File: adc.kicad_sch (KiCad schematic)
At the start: 35 parts, among them U7 AD7177-2BRUZ, U70 TG2520SMN-16M-MCG, U75 OPA2189DGK

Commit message: Scan deleted.
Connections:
- net BufR+: no longer U7.22 (AIN1)
- net BufR-: no longer U7.23 (AIN2)
- no-connect marks 6 -> 8
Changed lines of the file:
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@@
 	)
 	(junction
-		(at 157.48 60.96)
-		(diameter 0)
-		(color 0 0 0 0)
-	)
-	(junction
-		(at 139.7 63.5)
-		(diameter 0)
-		(color 0 0 0 0)
-	)
-	(junction
 		(at 97.79 86.36)
 		(diameter 0)
@@
 	)
 	(no_connect
+		(at 168.91 48.26)
+	)
+	(no_connect
 		(at 199.39 63.5)
 	)
 	(no_connect
+		(at 168.91 50.8)
+	)
+	(no_connect
 		(at 199.39 45.72)
 	)
@@
 	(wire
 		(pts
-			(xy 139.7 48.26) (xy 139.7 63.5)
-		)
-		(stroke
-			(width 0)
-			(type default)
-		)
-	)
-	(wire
-		(pts
 			(xy 101.6 96.52) (xy 116.84 96.52)
 		)
@@
 	(wire
 		(pts
-			(xy 142.24 60.96) (xy 157.48 60.96)
+			(xy 142.24 60.96) (xy 168.91 60.96)
 		)
 		(stroke
@@
 	(wire
 		(pts
-			(xy 157.48 60.96) (xy 168.91 60.96)
-		)
-		(stroke
-			(width 0)
-			(type default)
-		)
-	)
-	(wire
-		(pts
 			(xy 91.44 86.36) (xy 97.79 86.36)
 		)
@@
 	(wire
 		(pts
-			(xy 157.48 50.8) (xy 157.48 60.96)
-		)
-		(stroke
-			(width 0)
-			(type default)
-		)
-	)
-	(wire
-		(pts
 			(xy 134.62 118.11) (xy 139.7 118.11)
 		)
@@
 	(wire
 		(pts
-			(xy 139.7 63.5) (xy 168.91 63.5)
-		)
-		(stroke
-			(width 0)
-			(type default)
-		)
-	)
-	(wire
-		(pts
 			(xy 200.66 48.26) (xy 214.63 48.26)
 		)
@@
 	(wire
 		(pts
-			(xy 139.7 48.26) (xy 168.91 48.26)
-		)
-		(stroke
-			(width 0)
-			(type default)
-		)
-	)
-	(wire
-		(pts
 			(xy 199.39 68.58) (xy 203.2 68.58)
 		)
@@
 	(wire
 		(pts
-			(xy 157.48 50.8) (xy 168.91 50.8)
-		)
-		(stroke
-			(width 0)
-			(type default)
-		)
-	)
-	(wire
-		(pts
 			(xy 175.26 105.41) (xy 186.69 105.41)
 		)
@@
 	(wire
 		(pts
-			(xy 135.89 63.5) (xy 139.7 63.5)
+			(xy 135.89 63.5) (xy 168.91 63.5)
 		)
 		(stroke
@@
 			)
 		)
-		(property "Datasheet" "50V"
+		(property "Datasheet" "X7R, 50V"
 			(at 139.7 106.68 0)
 			(effects
@@
 			)
 		)
-		(property "Datasheet" "50V"
+		(property "Datasheet" "X7R, 50V"
 			(at 139.7 114.3 0)
 			(effects

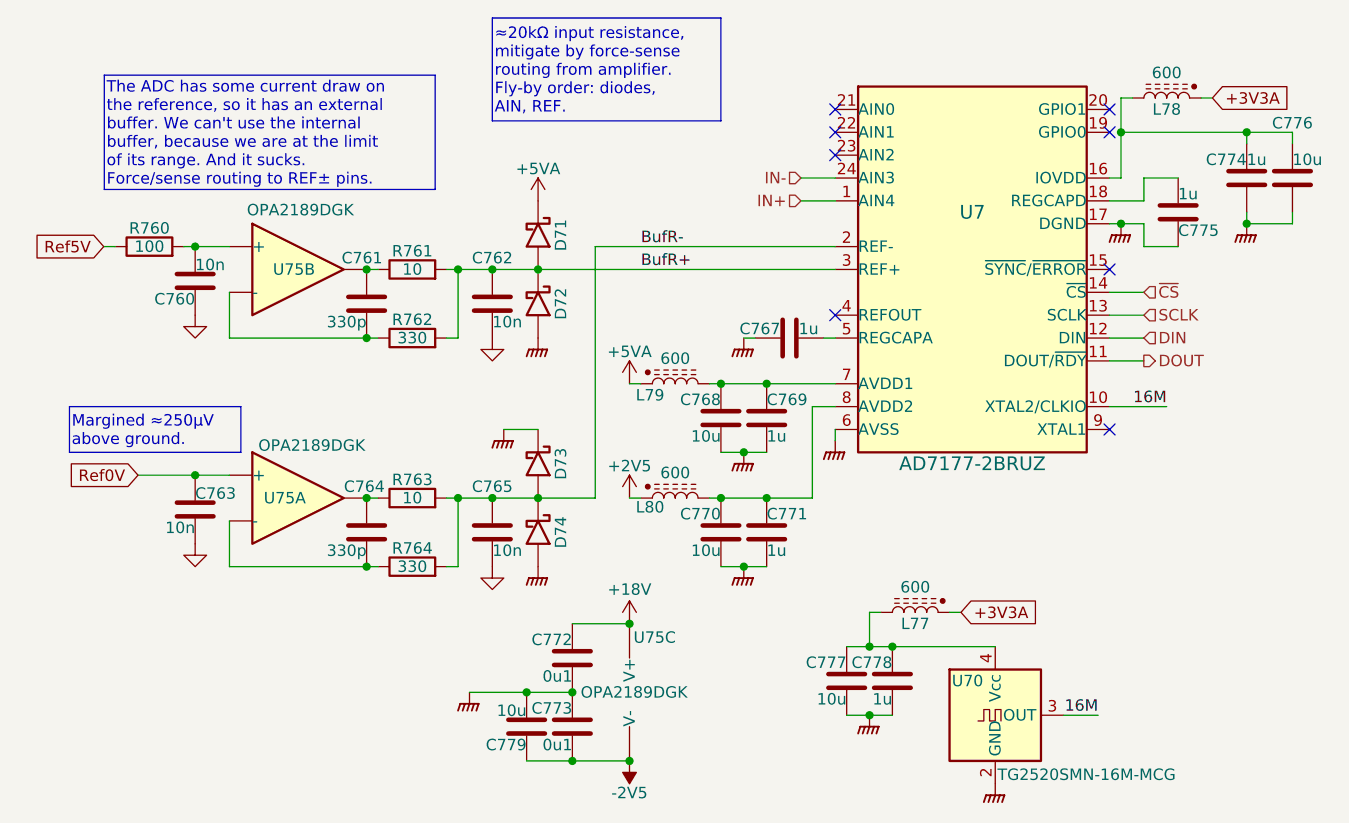
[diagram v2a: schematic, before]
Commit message: Put ref filtering into the schematic.
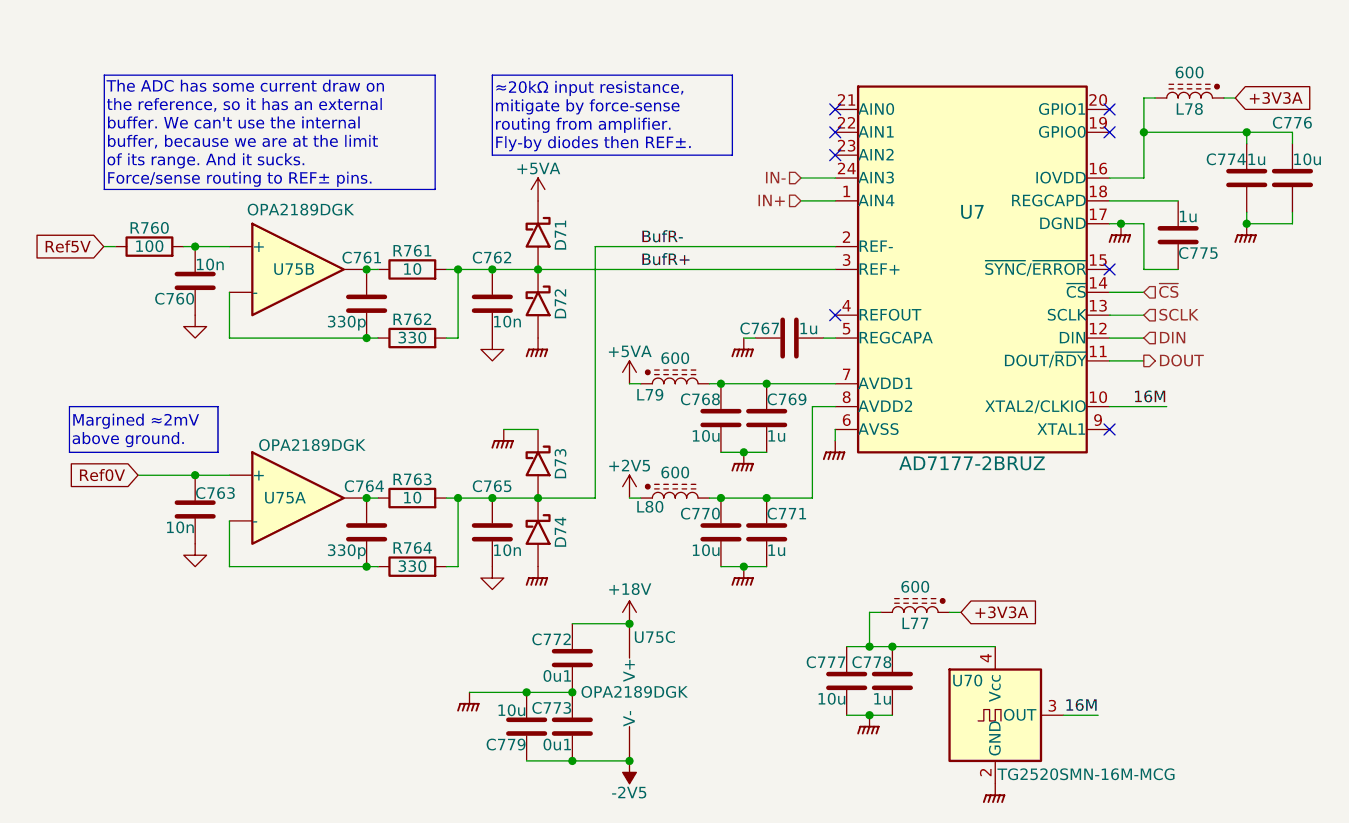
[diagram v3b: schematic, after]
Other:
- moved on the sheet: C775, L78
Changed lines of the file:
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@@
 	(generator_version "9.0")
 	(paper "A4")
-	(text_box "Margined ≈250µV above ground."
+	(text_box "Margined ≈2mV above ground."
 		(exclude_from_sim no)
 		(at 83.82 78.74 0)
-		(size 19.05 5.08)
+		(size 16.51 5.08)
 		(margins 0.254 0.254 0.254 0.254)
 		(stroke
@@
 		)
 	)
-	(text_box "≈20kΩ input resistance, mitigate by force-sense routing from amplifier.\nFly-by order: diodes, AIN, REF."
+	(text_box "≈20kΩ input resistance, mitigate by force-sense routing from amplifier.\nFly-by diodes then REF±."
 		(exclude_from_sim no)
-		(at 130.81 35.56 0)
-		(size 25.4 11.43)
+		(at 130.81 41.91 0)
+		(size 26.67 8.89)
 		(margins 0.254 0.254 0.254 0.254)
 		(stroke
@@
 	)
 	(junction
-		(at 200.66 48.26)
-		(diameter 0)
-		(color 0 0 0 0)
-	)
-	(junction
 		(at 214.63 48.26)
 		(diameter 0)
@@
 	)
 	(junction
+		(at 203.2 48.26)
+		(diameter 0)
+		(color 0 0 0 0)
+	)
+	(junction
 		(at 146.05 102.87)
 		(diameter 0)
@@
 	(wire
 		(pts
-			(xy 200.66 48.26) (xy 200.66 53.34)
+			(xy 203.2 48.26) (xy 203.2 53.34)
 		)
 		(stroke
@@
 	(wire
 		(pts
-			(xy 203.2 60.96) (xy 203.2 58.42)
+			(xy 203.2 63.5) (xy 203.2 58.42)
+		)
+		(stroke
+			(width 0)
+			(type default)
+		)
+	)
+	(wire
+		(pts
+			(xy 213.36 44.45) (xy 212.09 44.45)
 		)
 		(stroke
@@
 	(wire
 		(pts
-			(xy 210.82 44.45) (xy 209.55 44.45)
+			(xy 203.2 48.26) (xy 214.63 48.26)
 		)
 		(stroke
@@
 	(wire
 		(pts
-			(xy 200.66 53.34) (xy 199.39 53.34)
+			(xy 203.2 53.34) (xy 199.39 53.34)
 		)
 		(stroke
@@
 	(wire
 		(pts
-			(xy 203.2 53.34) (xy 207.01 53.34)
-		)
-		(stroke
-			(width 0)
-			(type default)
-		)
-	)
-	(wire
-		(pts
 			(xy 214.63 57.15) (xy 214.63 58.42)
 		)
@@
 	(wire
 		(pts
-			(xy 199.39 55.88) (xy 203.2 55.88)
+			(xy 199.39 55.88) (xy 207.01 55.88)
 		)
 		(stroke
@@
 	(wire
 		(pts
-			(xy 203.2 60.96) (xy 207.01 60.96)
+			(xy 203.2 63.5) (xy 207.01 63.5)
 		)
 		(stroke
@@
 	(wire
 		(pts
-			(xy 203.2 55.88) (xy 203.2 53.34)
-		)
-		(stroke
-			(width 0)
-			(type default)
-		)
-	)
-	(wire
-		(pts
 			(xy 168.91 82.55) (xy 168.91 81.28)
 		)
@@
 	(wire
 		(pts
-			(xy 200.66 44.45) (xy 200.66 48.26)
+			(xy 203.2 44.45) (xy 203.2 48.26)
 		)
 		(stroke
@@
 	(wire
 		(pts
-			(xy 200.66 48.26) (xy 214.63 48.26)
-		)
-		(stroke
-			(width 0)
-			(type default)
-		)
-	)
-	(wire
-		(pts
 			(xy 135.89 88.9) (xy 142.24 88.9)
 		)
@@
 	(wire
 		(pts
-			(xy 200.66 44.45) (xy 201.93 44.45)
+			(xy 203.2 44.45) (xy 204.47 44.45)
 		)
 		(stroke
@@
 	(global_label "+3V3A"
 		(shape input)
-		(at 210.82 44.45 0)
+		(at 213.36 44.45 0)
 		(fields_autoplaced yes)
 		(effects
@@
 		)
 		(property "Intersheetrefs" "${INTERSHEET_REFS}"
-			(at 218.8852 44.45 0)
+			(at 221.4252 44.45 0)
 			(effects
 				(font
@@
 	(symbol
 		(lib_id "Device:C")
-		(at 207.01 57.15 0)
+		(at 207.01 59.69 0)
 		(unit 1)
 		(exclude_from_sim no)
@@
 		(dnp no)
 		(property "Reference" "C775"
-			(at 207.01 59.1819 0)
+			(at 207.01 61.7219 0)
 			(effects
 				(font
@@
 		)
 		(property "Value" "1u"
-			(at 207.01 55.1179 0)
+			(at 207.01 57.6579 0)
 			(effects
 				(font
@@
 		)
 		(property "Footprint" "Capacitor_SMD:C_0402_1005Metric"
-			(at 207.9752 60.96 0)
+			(at 207.9752 63.5 0)
 			(effects
 				(font
@@
 		)
 		(property "Datasheet" "25V"
-			(at 207.01 57.15 0)
+			(at 207.01 59.69 0)
 			(effects
 				(font
@@
 		)
 		(property "Description" "Unpolarized capacitor"
-			(at 207.01 57.15 0)
+			(at 207.01 59.69 0)
 			(effects
 				(font
@@
 		)
 		(property "LCSC" "C52923"
-			(at 207.01 57.15 0)
+			(at 207.01 59.69 0)
 			(effects
 				(font
@@
 		)
 		(property "Stock" ""
-			(at 207.01 57.15 0)
+			(at 207.01 59.69 0)
 			(effects
 				(font
@@
 	(symbol
 		(lib_id "Parts:L_Ferrite_Power")
-		(at 205.74 44.45 270)
+		(at 208.28 44.45 270)
 		(mirror x)
 		(unit 1)
@@
 		(dnp no)
 		(property "Reference" "L78"
-			(at 205.74 45.72 90)
+			(at 208.28 45.72 90)
 			(effects
 				(font
@@
 		)
 		(property "Value" "600"
-			(at 205.74 41.656 90)
+			(at 208.28 41.656 90)
 			(effects
 				(font
@@
 		)
 		(property "Footprint" "Inductor_SMD:L_0603_1608Metric"
-			(at 205.74 44.45 0)
+			(at 208.28 44.45 0)
 			(effects
 				(font
@@
 		)
 		(property "Datasheet" "200mA / 450mΩ"
-			(at 205.74 44.45 0)
+			(at 208.28 44.45 0)
 			(effects
 				(font
@@
 		)
 		(property "Description" "Inductor with ferrite core"
-			(at 205.74 44.45 0)
+			(at 208.28 44.45 0)
 			(effects
 				(font
@@
 		)
 		(property "LCSC" "C1002"
-			(at 205.74 44.45 90)
+			(at 208.28 44.45 90)
 			(effects
 				(font
@@
 		)
 		(property "Stock" ""
-			(at 205.74 44.45 90)
+			(at 208.28 44.45 90)
 			(effects
 				(font

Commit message: Adjust voltage rails.
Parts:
- D71, D72, D73, D74: footprint Diode_SMD:D_SOD-323 -> Parts:SOD-323
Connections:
- net +18V renamed +19V
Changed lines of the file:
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@@
 			)
 		)
-		(property "Footprint" "Diode_SMD:D_SOD-323"
+		(property "Footprint" "Parts:SOD-323"
 			(at 131.445 92.71 0)
 			(effects
@@
 			)
 		)
-		(property "Footprint" "Diode_SMD:D_SOD-323"
+		(property "Footprint" "Parts:SOD-323"
 			(at 131.445 67.31 0)
 			(effects
@@
 			)
 		)
-		(property "Footprint" "Diode_SMD:D_SOD-323"
+		(property "Footprint" "Parts:SOD-323"
 			(at 131.445 59.69 0)
 			(effects
@@
 			)
 		)
-		(property "Footprint" "Diode_SMD:D_SOD-323"
+		(property "Footprint" "Parts:SOD-323"
 			(at 131.445 85.09 0)
 			(effects
@@
 	)
 	(symbol
-		(lib_id "Parts:+18V")
+		(lib_id "Parts:+19V")
 		(at 146.05 102.87 0)
 		(unit 1)
@@
 		(on_board yes)
 		(dnp no)
-		(property "Reference" "#PWR0761"
+		(property "Reference" "#PWR761"
 			(at 146.05 106.68 0)
 			(effects
@@
 			)
 		)
-		(property "Value" "+18V"
-			(at 146.05 99.06 0)
+		(property "Value" "+19V"
+			(at 146.05 99.314 0)
 			(do_not_autoplace yes)
 			(effects
@@
 			)
 		)
-		(property "Description" "Power symbol creates a global label with name {dblquote}+18V{dblquote}"
+		(property "Description" "Power symbol creates a global label with name \"+19\""
 			(at 146.05 102.87 0)
 			(effects
@@
 			(project "lincal"
 				(path "/b054cef4-39e3-49d8-aff0-7ba5a206c187/e69ade03-efa5-476d-a99a-7096b679a0cf"
-					(reference "#PWR0761")
+					(reference "#PWR761")
 					(unit 1)
 				)

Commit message: Progress checkin.  About to redo FDA feedback again.
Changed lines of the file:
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@@
 		(lib_id "Device:C")
 		(at 214.63 53.34 0)
-		(mirror y)
 		(unit 1)
 		(exclude_from_sim no)
@@
 					(size 1.27 1.27)
 				)
-				(justify left)
+				(justify right)
 			)
 		)
@@
 					(size 1.27 1.27)
 				)
-				(justify right)
+				(justify left)
 			)
 		)
 		(property "Footprint" "Capacitor_SMD:C_0402_1005Metric"
-			(at 213.6648 57.15 0)
+			(at 215.5952 57.15 0)
 			(effects
 				(font

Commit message: Nearly all routed.  Repinning FDA resistors.
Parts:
- removed C763: 10n, Capacitor_SMD:C_0603_1608Metric, symbol Device:C
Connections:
- net Ref0V is gone; now on net GND: U75.3 (+)
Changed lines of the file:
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@@
 	)
 	(junction
-		(at 97.79 86.36)
-		(diameter 0)
-		(color 0 0 0 0)
-	)
-	(junction
 		(at 127 63.5)
 		(diameter 0)
@@
 	(wire
 		(pts
-			(xy 91.44 86.36) (xy 97.79 86.36)
-		)
-		(stroke
-			(width 0)
-			(type default)
-		)
-	)
-	(wire
-		(pts
 			(xy 156.21 76.2) (xy 161.29 76.2)
 		)
@@
 	(wire
 		(pts
-			(xy 97.79 86.36) (xy 101.6 86.36)
+			(xy 99.06 86.36) (xy 101.6 86.36)
 		)
 		(stroke
@@
 		)
 	)
-	(global_label "Ref0V"
-		(shape input)
-		(at 91.44 86.36 180)
-		(effects
-			(font
-				(size 1.27 1.27)
-			)
-			(justify right)
-		)
-		(property "Intersheetrefs" "${INTERSHEET_REFS}"
-			(at 84.8504 86.36 0)
-			(effects
-				(font
-					(size 1.27 1.27)
-				)
-				(justify right)
-			)
-		)
-	)
 	(global_label "Ref5V"
 		(shape input)
@@
 	(symbol
 		(lib_id "Device:C")
-		(at 97.79 90.17 0)
-		(unit 1)
-		(exclude_from_sim no)
-		(in_bom yes)
-		(on_board yes)
-		(dnp no)
-		(property "Reference" "C763"
-			(at 97.79 88.392 0)
-			(effects
-				(font
-					(size 1.27 1.27)
-				)
-				(justify left)
-			)
-		)
-		(property "Value" "10n"
-			(at 97.79 92.202 0)
-			(effects
-				(font
-					(size 1.27 1.27)
-				)
-				(justify right)
-			)
-		)
-		(property "Footprint" "Capacitor_SMD:C_0603_1608Metric"
-			(at 98.7552 93.98 0)
-			(effects
-				(font
-					(size 1.27 1.27)
-				)
-				(hide yes)
-			)
-		)
-		(property "Datasheet" "C0G, 25V"
-			(at 97.79 90.17 0)
-			(effects
-				(font
-					(size 1.27 1.27)
-				)
-				(hide yes)
-			)
-		)
-		(property "Description" "Unpolarized capacitor"
-			(at 97.79 90.17 0)
-			(effects
-				(font
-					(size 1.27 1.27)
-				)
-				(hide yes)
-			)
-		)
-		(property "LCSC" "C307500"
-			(at 97.79 90.17 0)
-			(effects
-				(font
-					(size 1.27 1.27)
-				)
-				(hide yes)
-			)
-		)
-		(property "Stock" ""
-			(at 97.79 90.17 0)
-			(effects
-				(font
-					(size 1.27 1.27)
-				)
-				(hide yes)
-			)
-		)
-		(pin "1"
-		)
-		(pin "2"
-		)
-		(instances
-			(project "lincal"
-				(path "/b054cef4-39e3-49d8-aff0-7ba5a206c187/e69ade03-efa5-476d-a99a-7096b679a0cf"
-					(reference "C763")
-					(unit 1)
-				)
-			)
-		)
-	)
-	(symbol
-		(lib_id "Device:C")
 		(at 130.81 92.71 0)
 		(unit 1)
@@
 	(symbol
 		(lib_id "power:GND")
-		(at 97.79 93.98 0)
+		(at 99.06 86.36 0)
 		(unit 1)
 		(exclude_from_sim no)
@@
 		(dnp no)
 		(property "Reference" "#PWR0171"
-			(at 97.79 100.33 0)
+			(at 99.06 92.71 0)
 			(effects
 				(font
@@
 		)
 		(property "Value" "GND"
-			(at 97.79 97.79 0)
+			(at 99.06 90.17 0)
 			(effects
 				(font
@@
 		)
 		(property "Footprint" ""
-			(at 97.79 93.98 0)
+			(at 99.06 86.36 0)
 			(effects
 				(font
@@
 		)
 		(property "Datasheet" ""
-			(at 97.79 93.98 0)
+			(at 99.06 86.36 0)
 			(effects
 				(font
@@
 		)
 		(property "Description" "Power symbol creates a global label with name \"GND\" , ground"
-			(at 97.79 93.98 0)
+			(at 99.06 86.36 0)
 			(effects
 				(font

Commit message: DRC update.  Repin ADC.  De-crack the S/H ground.
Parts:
- renumbered C772 to C76
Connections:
- net IN+: now also U7.23 (AIN2); no longer U7.1 (AIN4)
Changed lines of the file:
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@@
 	)
 	(no_connect
+		(at 168.91 55.88)
+	)
+	(no_connect
 		(at 168.91 68.58)
 	)
@@
 	)
 	(no_connect
-		(at 168.91 50.8)
-	)
-	(no_connect
 		(at 199.39 45.72)
 	)
@@
 	(wire
 		(pts
-			(xy 165.1 55.88) (xy 168.91 55.88)
+			(xy 165.1 50.8) (xy 168.91 50.8)
 		)
 		(stroke
@@
 	(hierarchical_label "IN+"
 		(shape input)
-		(at 165.1 55.88 180)
+		(at 165.1 50.8 180)
 		(effects
 			(font
@@
 		(on_board yes)
 		(dnp no)
-		(property "Reference" "C772"
+		(property "Reference" "C76"
 			(at 139.7 104.648 0)
 			(effects
@@
 			(project "lincal"
 				(path "/b054cef4-39e3-49d8-aff0-7ba5a206c187/e69ade03-efa5-476d-a99a-7096b679a0cf"
-					(reference "C772")
+					(reference "C76")
 					(unit 1)
 				)

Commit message: More component metadata.
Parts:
- C76, C760, C761, C762, C764, C765, C767, C768, C769, C770, C771, C773, C774, C775, C776, C777, C778, C779, D71, D72, D73, D74, L77, L78, L79, L80, R760, R761, R762, R763, R764: Stock (none) -> JLC
- U70: Stock (none) -> ?
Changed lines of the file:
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@@
 			)
 		)
-		(property "Stock" ""
+		(property "Stock" "JLC"
 			(at 135.89 92.71 0)
 			(effects
@@
 			)
 		)
-		(property "Stock" ""
+		(property "Stock" "JLC"
 			(at 161.29 80.01 0)
 			(effects
@@
 			)
 		)
-		(property "Stock" ""
+		(property "Stock" "JLC"
 			(at 175.26 109.22 0)
 			(effects
@@
 			)
 		)
-		(property "Stock" ""
+		(property "Stock" "JLC"
 			(at 207.01 59.69 0)
 			(effects
@@
 			)
 		)
-		(property "Stock" ""
+		(property "Stock" "JLC"
 			(at 161.29 92.71 0)
 			(effects
@@
 			)
 		)
-		(property "Stock" ""
+		(property "Stock" "JLC"
 			(at 121.92 88.9 90)
 			(effects
@@
 			)
 		)
-		(property "Stock" ""
+		(property "Stock" "JLC"
 			(at 219.71 53.34 0)
 			(effects
@@
 			)
 		)
-		(property "Stock" ""
+		(property "Stock" "JLC"
 			(at 177.8 101.6 90)
 			(effects
@@
 			)
 		)
-		(property "Stock" ""
+		(property "Stock" "JLC"
 			(at 135.89 67.31 0)
 			(effects
@@
 			)
 		)
-		(property "Stock" ""
+		(property "Stock" "JLC"
 			(at 121.92 71.12 90)
 			(effects
@@
 			)
 		)
-		(property "Stock" ""
+		(property "Stock" "JLC"
 			(at 130.81 67.31 0)
 			(effects
@@
 			)
 		)
-		(property "Stock" ""
+		(property "Stock" "JLC"
 			(at 130.81 92.71 0)
 			(effects
@@
 			)
 		)
-		(property "Stock" ""
+		(property "Stock" "JLC"
 			(at 214.63 53.34 0)
 			(effects
@@
 			)
 		)
-		(property "Stock" ""
+		(property "Stock" "JLC"
 			(at 121.92 96.52 90)
 			(effects
@@
 			)
 		)
-		(property "Stock" ""
+		(property "Stock" "JLC"
 			(at 163.83 71.12 90)
 			(effects
@@
 			)
 		)
-		(property "Stock" ""
+		(property "Stock" "JLC"
 			(at 134.62 114.3 0)
 			(effects
@@
 			)
 		)
-		(property "Stock" ""
+		(property "Stock" "JLC"
 			(at 116.84 67.31 0)
 			(effects
@@
 			)
 		)
-		(property "Stock" ""
+		(property "Stock" "JLC"
 			(at 156.21 92.71 0)
 			(effects
@@
 			)
 		)
-		(property "Stock" ""
+		(property "Stock" "JLC"
 			(at 97.79 64.77 0)
 			(effects
@@
 			)
 		)
-		(property "Stock" ""
+		(property "Stock" "JLC"
 			(at 170.18 109.22 0)
 			(effects
@@
 			)
 		)
-		(property "Stock" ""
+		(property "Stock" "JLC"
 			(at 156.21 80.01 0)
 			(effects
@@
 			)
 		)
-		(property "Stock" ""
+		(property "Stock" "JLC"
 			(at 151.13 88.9 90)
 			(effects
@@
 			)
 		)
-		(property "Stock" ""
+		(property "Stock" "JLC"
 			(at 121.92 63.5 90)
 			(effects
@@
 			)
 		)
-		(property "Stock" ""
+		(property "Stock" "JLC"
 			(at 139.7 106.68 0)
 			(effects
@@
 			)
 		)
-		(property "Stock" ""
+		(property "Stock" "JLC"
 			(at 135.89 59.69 0)
 			(effects
@@
 			)
 		)
-		(property "Stock" ""
+		(property "Stock" "JLC"
 			(at 116.84 92.71 0)
 			(effects
@@
 			)
 		)
-		(property "Stock" ""
+		(property "Stock" "JLC"
 			(at 208.28 44.45 90)
 			(effects
@@
 			)
 		)
-		(property "Stock" ""
+		(property "Stock" "JLC"
 			(at 135.89 85.09 0)
 			(effects
@@
 			)
 		)
-		(property "Stock" ""
+		(property "Stock" "?"
 			(at 186.69 113.03 0)
 			(effects
@@
 			)
 		)
-		(property "Stock" ""
+		(property "Stock" "JLC"
 			(at 151.13 76.2 90)
 			(effects
@@
 			)
 		)
-		(property "Stock" ""
+		(property "Stock" "JLC"
 			(at 139.7 114.3 0)
 			(effects
@@
 			)
 		)
-		(property "Stock" ""
+		(property "Stock" "JLC"
 			(at 92.71 60.96 90)
 			(effects
